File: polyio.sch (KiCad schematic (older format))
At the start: 1 part

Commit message: Finished a breakout board, am not yet satisfied with the connector layout.
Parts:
- removed U?: CARAMBOLA, symbol CARAMBOLA
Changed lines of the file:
@@
-EESchema Schematic File Version 2  date Thu 14 Jun 2012 12:21:31 PM CEST
+EESchema Schematic File Version 2  date Tue 19 Jun 2012 03:03:41 PM CEST
 LIBS:power
 LIBS:device
@@
 LIBS:carambola
 LIBS:my-xilinx
+LIBS:arduino_shieldsNCL
 LIBS:polyio-cache
 EELAYER 25  0
 EELAYER END
-$Descr A4 11700 8267
+$Descr A2 23400 16535
 encoding utf-8
-Sheet 1 1
+Sheet 1 2
 Title ""
-Date "14 jun 2012"
+Date "19 jun 2012"
 Rev ""
 Comp ""
@@
 Comment4 ""
 $EndDescr
-$Comp
-L CARAMBOLA U?
-U 1 1 4FD9B57F
-P 2450 2550
-F 0 "U?" H 2450 2500 60  0000 C CNN
-F 1 "CARAMBOLA" H 2450 2600 60  0000 C CNN
-	1    2450 2550
-	1    0    0    -1
-$EndComp
+Wire Wire Line
+	7250 8100 7550 8100
+Wire Wire Line
+	7250 7450 7550 7450
+Wire Wire Line
+	9750 7250 9500 7250
+Wire Wire Line
+	7250 7350 7550 7350
+Wire Notes Line
+	17400 8000 17400 8050
+Wire Wire Line
+	7550 7250 7250 7250
+Wire Wire Line
+	9750 7150 9500 7150
+Wire Wire Line
+	7250 7150 7550 7150
+Text Label 7250 8100 0    60   ~ 0
+dout
+Text Label 7250 7450 0    60   ~ 0
+done
+Text Label 7250 7150 0    60   ~ 0
+init_b
+Text Label 9750 7150 2    60   ~ 0
+cb_rx
+Text Label 9750 7250 2    60   ~ 0
+cb_tx
+Text Label 7250 7350 0    60   ~ 0
+sck
+Text Label 7250 7250 0    60   ~ 0
+mosi
+$Sheet
+S 7550 7050 1950 1150
+U 4FDA1D6B
+F0 "fpga_io1" 60
+F1 "fpga_io.sch" 60
+F2 "tx" I R 9500 7150 60
+F3 "rx" I R 9500 7250 60
+F4 "init_b" I L 7550 7150 60
+F5 "mosi" I L 7550 7250 60
+F6 "dout" I L 7550 8100 60
+F7 "sck" I L 7550 7350 60
+F8 "done" I L 7550 7450 60
+$EndSheet
 $EndSCHEMATC

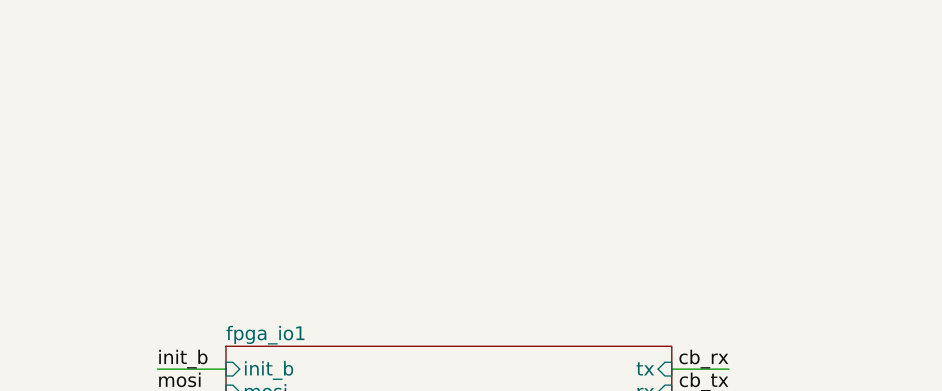
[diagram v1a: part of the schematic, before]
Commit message: Fixed the FPGAs decoupling & power supply. Started work towards output driver modules (to be connected via 10 pin cable).
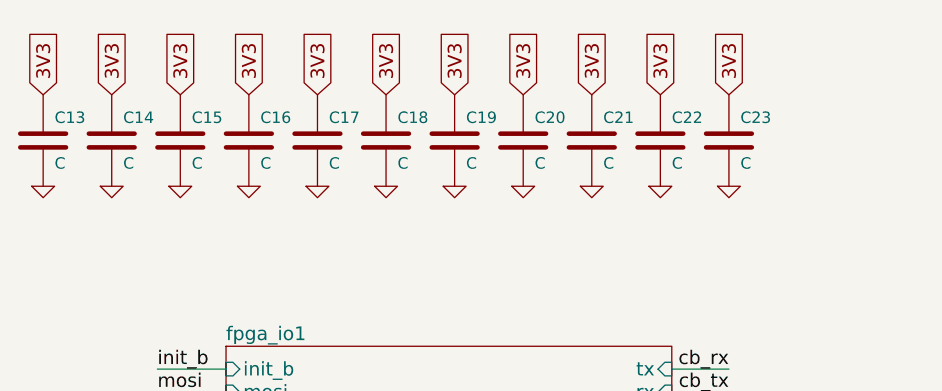
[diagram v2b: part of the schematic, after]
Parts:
- added C13, C14, C15, C16, C17, C18, C19, C20, C21, C22, C23: C, symbol C
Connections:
- new net 3V3: C13.1, C14.1, C15.1, C16.1, C17.1, C18.1, C19.1, C20.1, C21.1, C22.1, C23.1
- new net GND: C13.2, C14.2, C15.2, C16.2, C17.2, C18.2, C19.2, C20.2, C21.2, C22.2, C23.2
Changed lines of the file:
@@
-EESchema Schematic File Version 2  date Tue 19 Jun 2012 03:03:41 PM CEST
+EESchema Schematic File Version 2  date Fri 22 Jun 2012 01:24:32 AM CEST
 LIBS:power
 LIBS:device
@@
 Sheet 1 2
 Title ""
-Date "19 jun 2012"
+Date "21 jun 2012"
 Rev ""
 Comp ""
@@
 Comment4 ""
 $EndDescr
+Text GLabel 6750 5950 1    60   Input ~ 0
+3V3
+Text GLabel 7050 5950 1    60   Input ~ 0
+3V3
+Text GLabel 7350 5950 1    60   Input ~ 0
+3V3
+Text GLabel 7650 5950 1    60   Input ~ 0
+3V3
+Text GLabel 7950 5950 1    60   Input ~ 0
+3V3
+Text GLabel 8250 5950 1    60   Input ~ 0
+3V3
+Text GLabel 8550 5950 1    60   Input ~ 0
+3V3
+Text GLabel 8850 5950 1    60   Input ~ 0
+3V3
+Text GLabel 9150 5950 1    60   Input ~ 0
+3V3
+Text GLabel 9450 5950 1    60   Input ~ 0
+3V3
+Text GLabel 9750 5950 1    60   Input ~ 0
+3V3
+$Comp
+L GND #PWR11
+U 1 1 4FE23A74
+P 9750 6350
+F 0 "#PWR11" H 9750 6350 30  0001 C CNN
+F 1 "GND" H 9750 6280 30  0001 C CNN
+	1    9750 6350
+	1    0    0    -1
+$EndComp
+$Comp
+L GND #PWR10
+U 1 1 4FE23A72
+P 9450 6350
+F 0 "#PWR10" H 9450 6350 30  0001 C CNN
+F 1 "GND" H 9450 6280 30  0001 C CNN
+	1    9450 6350
+	1    0    0    -1
+$EndComp
+$Comp
+L GND #PWR9
+U 1 1 4FE23A6F
+P 9150 6350
+F 0 "#PWR9" H 9150 6350 30  0001 C CNN
+F 1 "GND" H 9150 6280 30  0001 C CNN
+	1    9150 6350
+	1    0    0    -1
+$EndComp
+$Comp
+L GND #PWR8
+U 1 1 4FE23A6D
+P 8850 6350
+F 0 "#PWR8" H 8850 6350 30  0001 C CNN
+F 1 "GND" H 8850 6280 30  0001 C CNN
+	1    8850 6350
+	1    0    0    -1
+$EndComp
+$Comp
+L GND #PWR7
+U 1 1 4FE23A6A
+P 8550 6350
+F 0 "#PWR7" H 8550 6350 30  0001 C CNN
+F 1 "GND" H 8550 6280 30  0001 C CNN
+	1    8550 6350
+	1    0    0    -1
+$EndComp
+$Comp
+L GND #PWR6
+U 1 1 4FE23A69
+P 8250 6350
+F 0 "#PWR6" H 8250 6350 30  0001 C CNN
+F 1 "GND" H 8250 6280 30  0001 C CNN
+	1    8250 6350
+	1    0    0    -1
+$EndComp
+$Comp
+L GND #PWR5
+U 1 1 4FE23A66
+P 7950 6350
+F 0 "#PWR5" H 7950 6350 30  0001 C CNN
+F 1 "GND" H 7950 6280 30  0001 C CNN
+	1    7950 6350
+	1    0    0    -1
+$EndComp
+$Comp
+L GND #PWR4
+U 1 1 4FE23A64
+P 7650 6350
+F 0 "#PWR4" H 7650 6350 30  0001 C CNN
+F 1 "GND" H 7650 6280 30  0001 C CNN
+	1    7650 6350
+	1    0    0    -1
+$EndComp
+$Comp
+L GND #PWR3
+U 1 1 4FE23A61
+P 7350 6350
+F 0 "#PWR3" H 7350 6350 30  0001 C CNN
+F 1 "GND" H 7350 6280 30  0001 C CNN
+	1    7350 6350
+	1    0    0    -1
+$EndComp
+$Comp
+L GND #PWR2
+U 1 1 4FE23A5E
+P 7050 6350
+F 0 "#PWR2" H 7050 6350 30  0001 C CNN
+F 1 "GND" H 7050 6280 30  0001 C CNN
+	1    7050 6350
+	1    0    0    -1
+$EndComp
+$Comp
+L GND #PWR1
+U 1 1 4FE23A5B
+P 6750 6350
+F 0 "#PWR1" H 6750 6350 30  0001 C CNN
+F 1 "GND" H 6750 6280 30  0001 C CNN
+	1    6750 6350
+	1    0    0    -1
+$EndComp
+$Comp
+L C C23
+U 1 1 4FE23A4E
+P 9750 6150
+F 0 "C23" H 9800 6250 50  0000 L CNN
+F 1 "C" H 9800 6050 50  0000 L CNN
+	1    9750 6150
+	1    0    0    -1
+$EndComp
+$Comp
+L C C22
+U 1 1 4FE23A4B
+P 9450 6150
+F 0 "C22" H 9500 6250 50  0000 L CNN
+F 1 "C" H 9500 6050 50  0000 L CNN
+	1    9450 6150
+	1    0    0    -1
+$EndComp
+$Comp
+L C C21
+U 1 1 4FE23A47
+P 9150 6150
+F 0 "C21" H 9200 6250 50  0000 L CNN
+F 1 "C" H 9200 6050 50  0000 L CNN
+	1    9150 6150
+	1    0    0    -1
+$EndComp
+$Comp
+L C C13
+U 1 1 4FE23A3E
+P 6750 6150
+F 0 "C13" H 6800 6250 50  0000 L CNN
+F 1 "C" H 6800 6050 50  0000 L CNN
+	1    6750 6150
+	1    0    0    -1
+$EndComp
+$Comp
+L C C14
+U 1 1 4FE23A3B
+P 7050 6150
+F 0 "C14" H 7100 6250 50  0000 L CNN
+F 1 "C" H 7100 6050 50  0000 L CNN
+	1    7050 6150
+	1    0    0    -1
+$EndComp
+$Comp
+L C C20
+U 1 1 4FE23A36
+P 8850 6150
+F 0 "C20" H 8900 6250 50  0000 L CNN
+F 1 "C" H 8900 6050 50  0000 L CNN
+	1    8850 6150
+	1    0    0    -1
+$EndComp
+$Comp
+L C C19
+U 1 1 4FE23A30
+P 8550 6150
+F 0 "C19" H 8600 6250 50  0000 L CNN
+F 1 "C" H 8600 6050 50  0000 L CNN
+	1    8550 6150
+	1    0    0    -1
+$EndComp
+$Comp
+L C C15
+U 1 1 4FE23A2D
+P 7350 6150
+F 0 "C15" H 7400 6250 50  0000 L CNN
+F 1 "C" H 7400 6050 50  0000 L CNN
+	1    7350 6150
+	1    0    0    -1
+$EndComp
+$Comp
+L C C18
+U 1 1 4FE23A24
+P 8250 6150
+F 0 "C18" H 8300 6250 50  0000 L CNN
+F 1 "C" H 8300 6050 50  0000 L CNN
+	1    8250 6150
+	1    0    0    -1
+$EndComp
+$Comp
+L C C17
+U 1 1 4FE23A20
+P 7950 6150
+F 0 "C17" H 8000 6250 50  0000 L CNN
+F 1 "C" H 8000 6050 50  0000 L CNN
+	1    7950 6150
+	1    0    0    -1
+$EndComp
+$Comp
+L C C16
+U 1 1 4FE23A1D
+P 7650 6150
+F 0 "C16" H 7700 6250 50  0000 L CNN
+F 1 "C" H 7700 6050 50  0000 L CNN
+	1    7650 6150
+	1    0    0    -1
+$EndComp
 Wire Wire Line
 	7250 8100 7550 8100
